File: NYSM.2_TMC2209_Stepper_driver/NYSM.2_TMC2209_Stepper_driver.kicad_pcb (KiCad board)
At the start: 2 copper layers, 22 x 28.5 mm, 19 parts, among them U1 TMC2209, U2 M.2-B-KEY

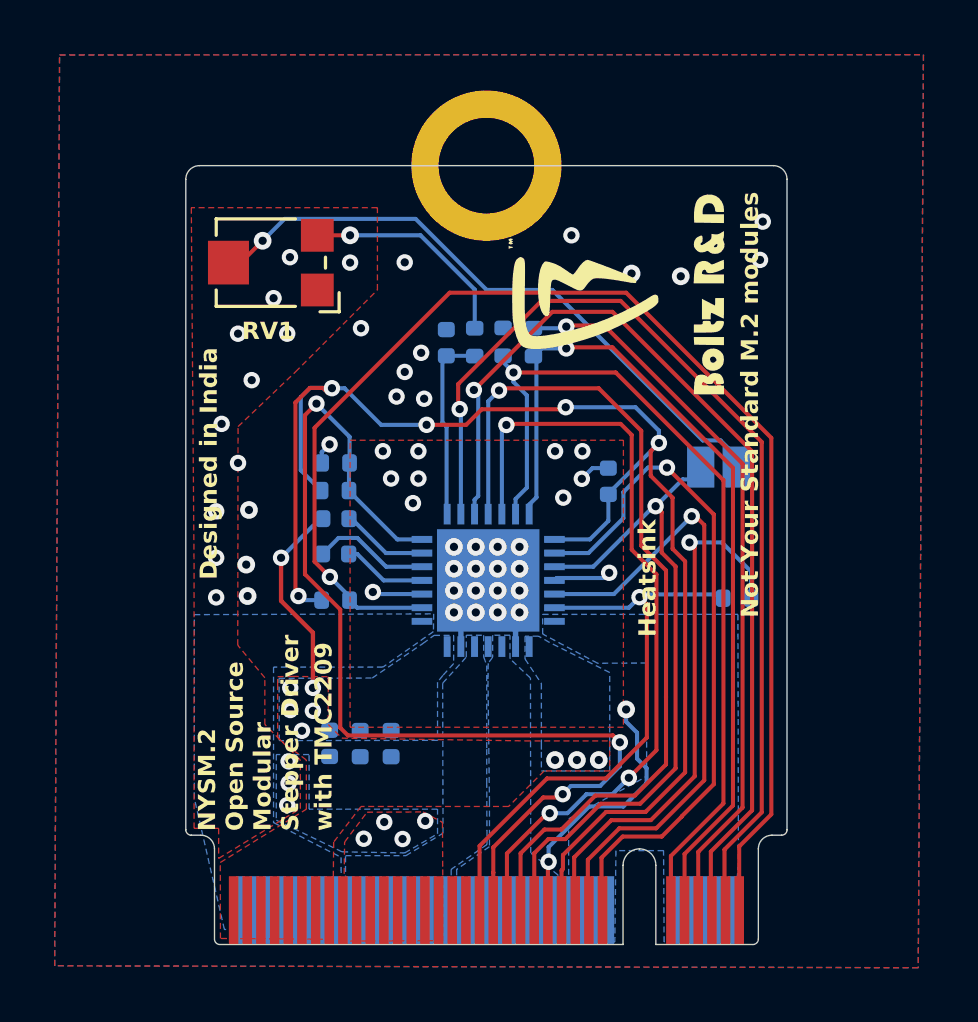
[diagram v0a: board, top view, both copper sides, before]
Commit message: Preliminary push for alternative version with External Sense Resistors
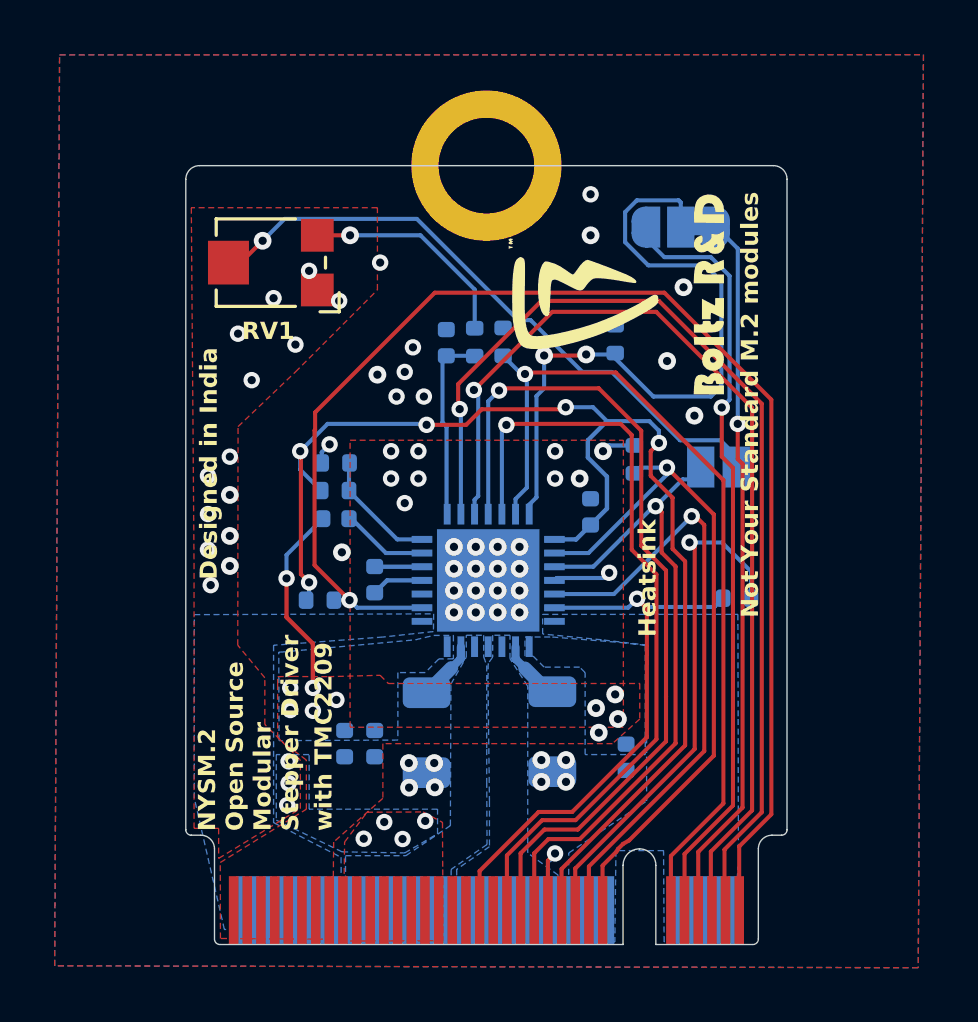
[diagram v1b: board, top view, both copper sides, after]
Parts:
- added JP2: UARTSel, Jumper:SolderJumper-3_P1.3mm_Bridged12_RoundedPad1.0x1.5mm, B.Cu at (151.9, 104.6)
- added R10: 20K, Resistor_SMD:R_0402_1005Metric, B.Cu at (150.2, 113.1)
- added R4: 0R100, Resistor_SMD:R_1206_3216Metric, B.Cu at (142.6, 123.1)
- added R5: 20K, Resistor_SMD:R_0402_1005Metric, B.Cu at (149.5, 108.7)
- R3: value 1K -> 0R100; footprint Resistor_SMD:R_0402_1005Metric -> Resistor_SMD:R_1206_3216Metric
- moved R3 14.3 mm to (147.2, 123.1), turned to 90 degrees
- moved C10 10.9 mm to (149.9, 124.0)
- moved C1 1.71 mm to (140.7, 117.5), turned to 90 degrees
- moved C8 1.70 mm to (139.6, 123.5)
- moved C6 1.29 mm to (148.6, 115.1)
- moved R1 0.57 mm to (138.7, 118.3)
- moved C9 0.53 mm to (140.7, 123.5)
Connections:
- R3 pad 1: UART_TX -> GND
- R3 pad 2: UART_RX -> Net-(U1-BRA)
- U1 pad 14: UART_RX -> Net-(JP2-C)
- U1 pad 23: GND -> Net-(U1-BRA)
- U1 pad 27: GND -> Net-(U1-BRB)
- U2 pad P$37: SPREAD -> SPREAD_NC
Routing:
- net SPREAD: track 38.9 -> 4.44 mm, vias 3 -> 0
- net Net-(JP2-C): track 0.00 -> 25.5 mm, vias 0 -> 2
- net GND: track 40.1 -> 27.1 mm, vias 63 -> 70
- net VCC_IO: track 54.8 -> 47.8 mm
- net UART_RX: track 32.4 -> 28.3 mm
- net Net-(U1-CPI): track 4.32 -> 1.73 mm
- net Net-(U1-BRB): track 0.00 -> 2.21 mm
- net Net-(U1-BRA): track 0.00 -> 2.21 mm
- net EN: track 48.3 -> 50.0 mm
- net Net-(U1-CPO): track 3.08 -> 1.92 mm
- net MS2: track 35.6 -> 36.5 mm
- net DIR: track 23.5 -> 22.6 mm
- net MS1: track 37.0 -> 37.8 mm
- net UART_TX: track 26.8 -> 26.1 mm
- net INDEX: track 29.4 -> 28.9 mm, vias 3 -> 1
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
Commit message: Added production Files
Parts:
- moved G*** 0.35 mm to (149.5, 107.3)
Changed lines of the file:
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@@
 	(footprint "Logo:BoltzRndLogo10mm"
 		(layer "F.Cu")
-		(at 149.490304 106.9492 90)
+		(at 149.490304 107.3 90)
 		(property "Reference" "G***"
 			(at 5.6 1.5 90)
@@
 			(effects
 				(font
-					(size 1 1)
-					(thickness 0.15)
+					(size 0.5 0.5)
+					(thickness 0.125)
+					(bold yes)
 				)
 				(justify mirror)
@@
 		)
 		(property "Value" "UARTSel"
-			(at 0 -1.9 360)
+			(at 0 -1.9 0)
 			(layer "B.Fab")
 			(effects
